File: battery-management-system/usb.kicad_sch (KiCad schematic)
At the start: 20 parts, among them J7 AMPHENOL_micro_usb_10118194-0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, U3 FT230XS

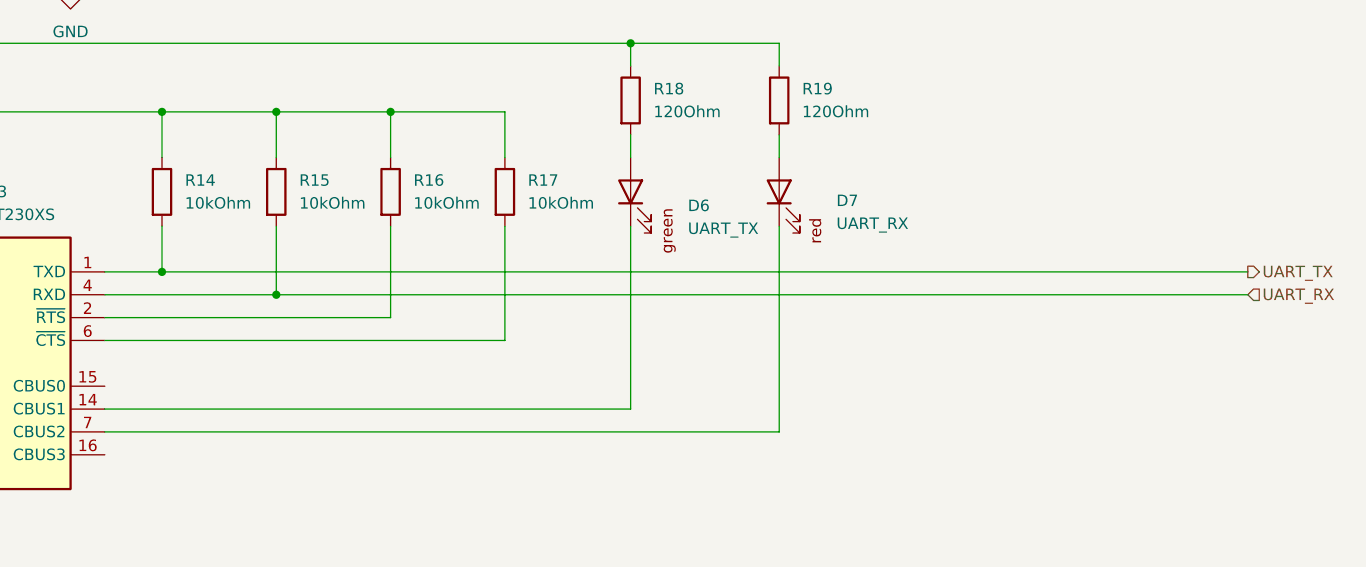
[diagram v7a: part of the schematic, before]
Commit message: implement interconnect
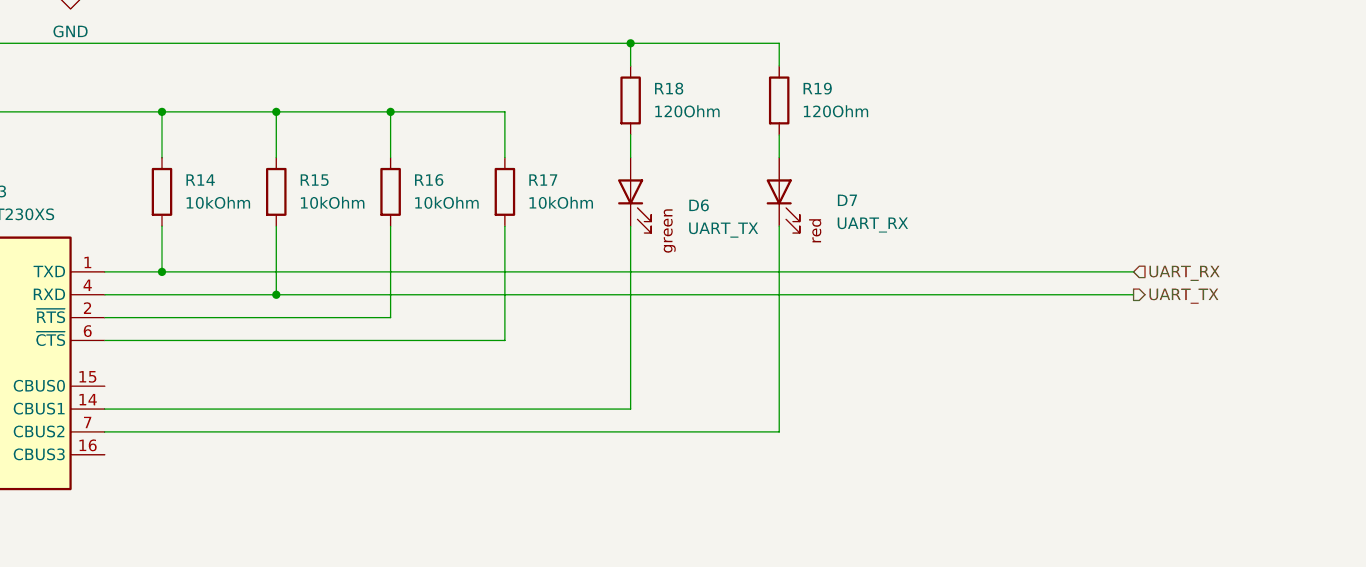
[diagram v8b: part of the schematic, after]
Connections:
- net UART_RX: now also R14.2, U3.1 (TXD); no longer R15.2, U3.4 (RXD)
- net UART_TX: now also R15.2, U3.4 (RXD); no longer R14.2, U3.1 (TXD)
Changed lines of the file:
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@@
   (junction (at 175.26 67.31) (diameter 0) (color 0 0 0 0)
   )
+  (junction (at 101.6 100.33) (diameter 0) (color 0 0 0 0)
+  )
+  (junction (at 72.39 73.66) (diameter 0) (color 0 0 0 0)
+  )
+  (junction (at 83.82 73.66) (diameter 0) (color 0 0 0 0)
+  )
+  (junction (at 74.93 92.71) (diameter 0) (color 0 0 0 0)
+  )
+  (junction (at 72.39 36.83) (diameter 0) (color 0 0 0 0)
+  )
+  (junction (at 162.56 87.63) (diameter 0) (color 0 0 0 0)
+  )
+  (junction (at 72.39 59.69) (diameter 0) (color 0 0 0 0)
+  )
+  (junction (at 149.86 67.31) (diameter 0) (color 0 0 0 0)
+  )
+  (junction (at 139.7 39.37) (diameter 0) (color 0 0 0 0)
+  )
+  (junction (at 96.52 73.66) (diameter 0) (color 0 0 0 0)
+  )
   (junction (at 149.86 85.09) (diameter 0) (color 0 0 0 0)
   )
-  (junction (at 101.6 100.33) (diameter 0) (color 0 0 0 0)
-  )
-  (junction (at 72.39 73.66) (diameter 0) (color 0 0 0 0)
-  )
-  (junction (at 83.82 73.66) (diameter 0) (color 0 0 0 0)
-  )
-  (junction (at 162.56 87.63) (diameter 0) (color 0 0 0 0)
-  )
-  (junction (at 74.93 92.71) (diameter 0) (color 0 0 0 0)
-  )
-  (junction (at 72.39 36.83) (diameter 0) (color 0 0 0 0)
-  )
-  (junction (at 72.39 59.69) (diameter 0) (color 0 0 0 0)
-  )
-  (junction (at 149.86 67.31) (diameter 0) (color 0 0 0 0)
-  )
-  (junction (at 139.7 39.37) (diameter 0) (color 0 0 0 0)
-  )
-  (junction (at 96.52 73.66) (diameter 0) (color 0 0 0 0)
-  )
   (junction (at 123.19 115.57) (diameter 0) (color 0 0 0 0)
   )
@@
     (stroke (width 0) (type default) (color 0 0 0 0))
   )
-  (wire (pts (xy 149.86 85.09) (xy 270.51 85.09))
-    (stroke (width 0) (type default) (color 0 0 0 0))
-  )
   (wire (pts (xy 72.39 59.69) (xy 72.39 73.66))
     (stroke (width 0) (type default) (color 0 0 0 0))
@@
     (stroke (width 0) (type default) (color 0 0 0 0))
   )
+  (wire (pts (xy 149.86 85.09) (xy 257.81 85.09))
+    (stroke (width 0) (type default) (color 0 0 0 0))
+  )
   (wire (pts (xy 149.86 80.01) (xy 149.86 85.09))
     (stroke (width 0) (type default) (color 0 0 0 0))
@@
     (stroke (width 0) (type default) (color 0 0 0 0))
   )
+  (wire (pts (xy 257.81 87.63) (xy 162.56 87.63))
+    (stroke (width 0) (type default) (color 0 0 0 0))
+  )
   (wire (pts (xy 175.26 67.31) (xy 175.26 72.39))
     (stroke (width 0) (type default) (color 0 0 0 0))
@@
     (stroke (width 0) (type default) (color 0 0 0 0))
   )
-  (wire (pts (xy 162.56 87.63) (xy 270.51 87.63))
-    (stroke (width 0) (type default) (color 0 0 0 0))
-  )
   (wire (pts (xy 201.93 100.33) (xy 143.51 100.33))
     (stroke (width 0) (type default) (color 0 0 0 0))
@@
     (stroke (width 0) (type default) (color 0 0 0 0))
   )
-  (hierarchical_label "UART_TX" (shape output) (at 270.51 85.09 0)
+  (hierarchical_label "UART_TX" (shape output) (at 257.81 87.63 0)
     (effects (font (size 1.27 1.27)) (justify left))
   )
-  (hierarchical_label "UART_RX" (shape input) (at 270.51 87.63 0)
+  (hierarchical_label "UART_RX" (shape input) (at 257.81 85.09 0)
     (effects (font (size 1.27 1.27)) (justify left))
   )
